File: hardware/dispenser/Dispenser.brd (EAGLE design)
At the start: 73.7 x 75.6 mm, 64 parts, among them J1 AVR_Prog, J2 RJ45-8PTH, Q1 NFET-SO8, Q2 NFET, Q3 NFET, Q4 NFET, Q5 MOSFET-NCHANNELSMD, U1 ATMEGA168, U10 HALL-EFFECT, U2 OPAMP-DUAL, U3 OPTO-TLP185, U4 MPX10DP, U5 VREG-5V-LDO-AP1117SOT89-3L, U6 WS2801, U7 HALL-EFFECT, U8 HALL-EFFECT, U9 HALL-EFFECT

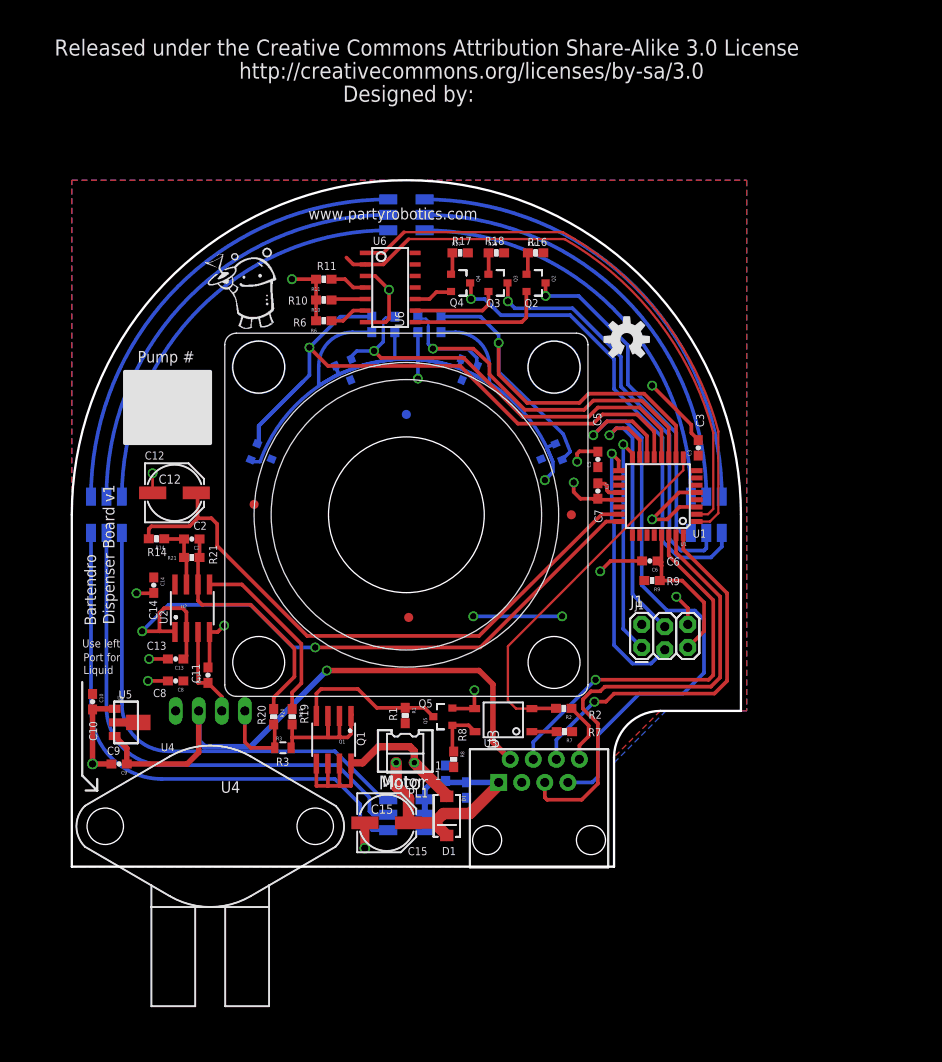
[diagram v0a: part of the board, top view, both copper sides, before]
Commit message: Checking in the final dispenser schematics for the kickstarter dispensers
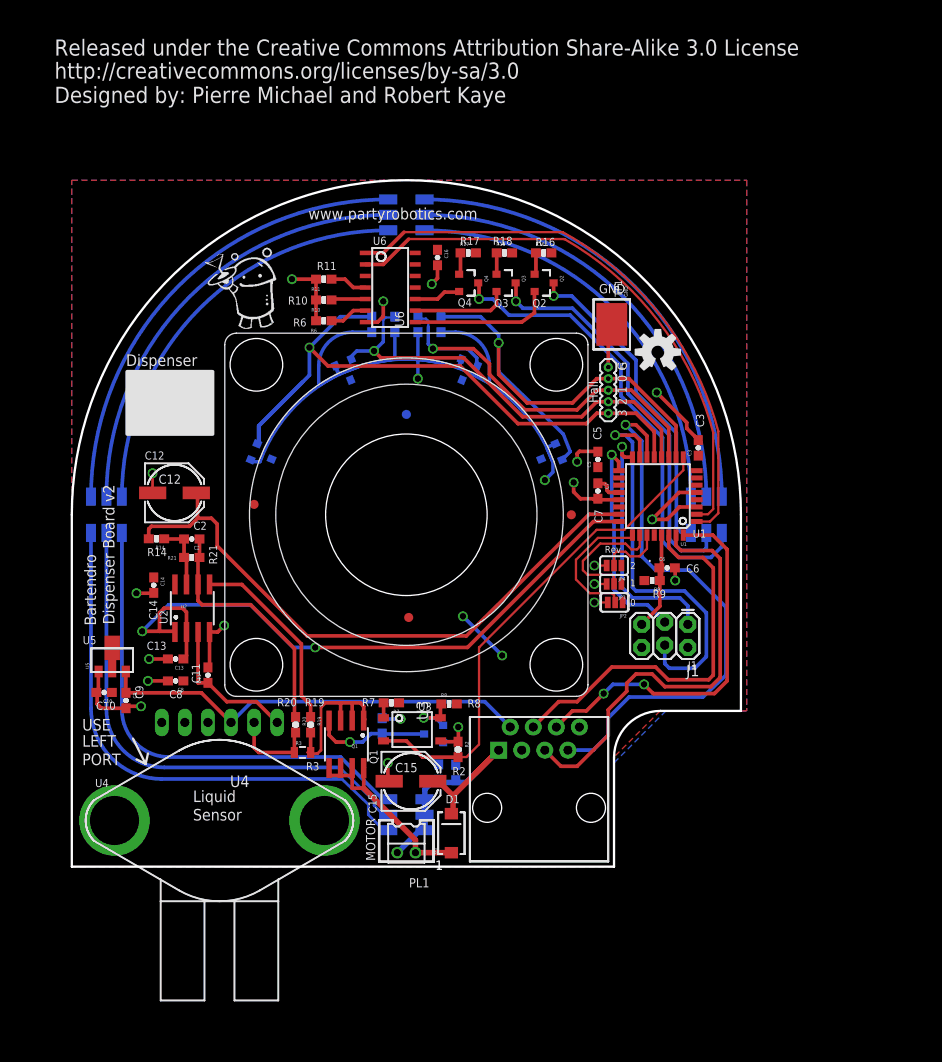
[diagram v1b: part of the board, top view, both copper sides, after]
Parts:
- added C16: 100n, SparkFun:0603-CAP
- added JP1: (no value), SparkFun:1X05-1.27MM
- added JP2, JP4: JUMPER-32-3, SparkFun-Passives:SJ_3_PASTE2&3
- added JP3: JUMPER-31-2, SparkFun-Passives:SJ_3_PASTE1&2
- added TP1: GND, microbuilder:TESTPOINT_SMT
- J2: device SparkFun:RJ45-8 -> pierre:RJ45-8
- PL1: device con-hirose-df3:DF3P-02 -> pierre:DF3P-02
- U4: value MPX10DP -> MPX5010DP; device pierre:CASE344C-01 -> pierre:MPX5010DP
- moved R7 19.3 mm to (35.2, 18.0)
- moved R2 12.5 mm to (42.5, 12.9), turned to 270 degrees
- moved U3 10.1 mm to (37.5, 15.1), turned to 270 degrees
- moved PL1 9.91 mm to (36.8, 2.54)
- moved C9 7.03 mm to (5.97, 18.3), turned to 270 degrees
- moved U5 7.03 mm to (4.45, 22.7), turned to 0 degrees
- moved R8 6.12 mm to (41.5, 17.9), turned to 0 degrees
- moved J1 5.68 mm to (67.8, 26.7), turned to 180 degrees
- moved C15 5.29 mm to (37.3, 9.40)
- moved U$1 3.70 mm to (64.5, 56.6)
- moved J2 3.56 mm to (51.4, 6.48)
- moved R1 2.79 mm to (34.2, 15.5), flipped to the bottom, turned to 90 degrees
- moved R20 2.57 mm to (24.6, 15.6)
- moved C4 2.27 mm to (42.3, 10.4), turned to 90 degrees
- moved R19 2.22 mm to (26.3, 15.6)
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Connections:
- new net R0: JP2.2, U1.25
- new net R1: JP3.2, U1.26
- new net R2: JP4.2, U1.27
- net 3.3V: now also C16.1, JP2.1, JP3.1, JP4.1
- net GND: now also C16.2, JP1.1, JP2.3, JP3.3, JP4.3, TP1.P$1, U4.2; no longer U4.1, U6.3
- net HALL0: now also JP1.2
- net HALL1: now also JP1.3
- net HALL2: now also JP1.4
- net HALL3: now also JP1.5
- net N$26: now also U4.1; no longer U4.2
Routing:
- net 5V: track 65.7 -> 48.1 mm, vias 1 -> 0
- net R0: track 0.00 -> 15.5 mm
- net R1: track 0.00 -> 14.3 mm
- net MOT_CTL: track 40.5 -> 54.5 mm
- net MOSI: track 31.6 -> 44.5 mm
- net GND: track 103.9 -> 92.1 mm, vias 16 -> 19
- net SYNC: track 69.4 -> 61.4 mm
- net R2: track 0.00 -> 7.06 mm
- net SCK: track 30.4 -> 24.1 mm
- net N$26: track 10.4 -> 16.1 mm
- net !RST: track 17.7 -> 12.0 mm
- net TX: track 52.1 -> 47.1 mm
- net MOT_B: track 28.1 -> 23.6 mm
- net N$9: track 16.8 -> 12.8 mm, vias 0 -> 1
- net MISO: track 25.0 -> 28.1 mm
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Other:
- board text added: "0"
- board text added: "2"
- board text added: "3"
- board text added: "C16"
- board text added: "Designed by: Pierre Michael and Robert Kaye"
- board text added: "Dispenser"
- board text added: "Dispenser Board v2"
- board text added: "G"
- board text added: "GND"
- board text added: "Hall"
- board text added: "JP1"
- board text added: "LEFT"
- board text added: "MOTOR"
- board text added: "PL1"
- board text added: "PORT"
- board text added: "Rev"
- board text added: "Sensor"
- board text added: "TP1"
- board text added: "USE"
- board text removed: "Designed by:"
- board text removed: "Dispenser Board v1"
- board text removed: "Motor"
- board text removed: "Port for"
- board text removed: "Pump #"
- board text removed: "Use left"
